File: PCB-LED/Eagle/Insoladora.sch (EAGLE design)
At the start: 62 parts

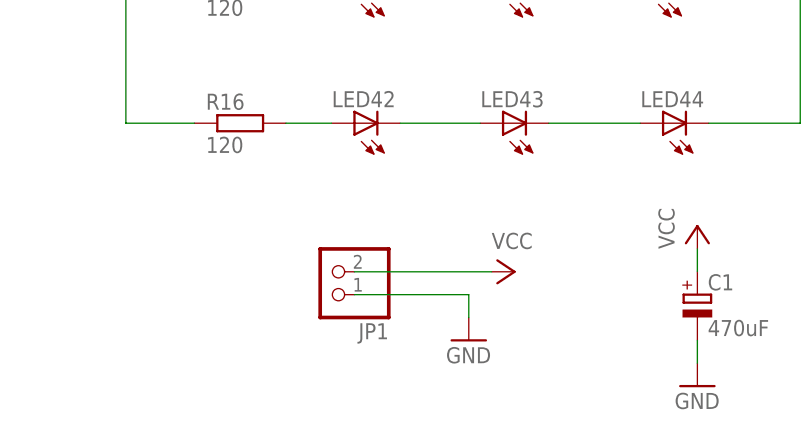
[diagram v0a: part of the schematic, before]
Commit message: Board v1.3
Added new power supply connector and bigger pads for ease soldering
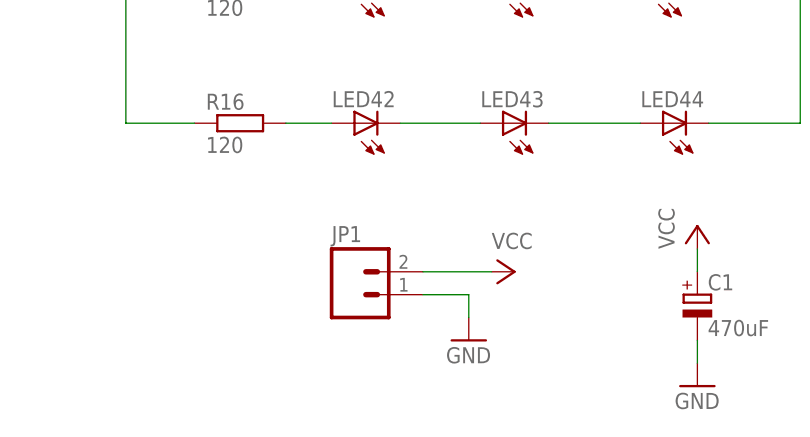
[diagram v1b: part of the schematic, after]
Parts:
- JP1: device pinhead:PINHD-1X2 -> SparkFun-Connectors:M023.5MM_LOCK
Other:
- moved on the sheet: JP1
